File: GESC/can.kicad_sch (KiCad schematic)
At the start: 7 parts, among them J8 CAN, U5 SN65HVD230DR

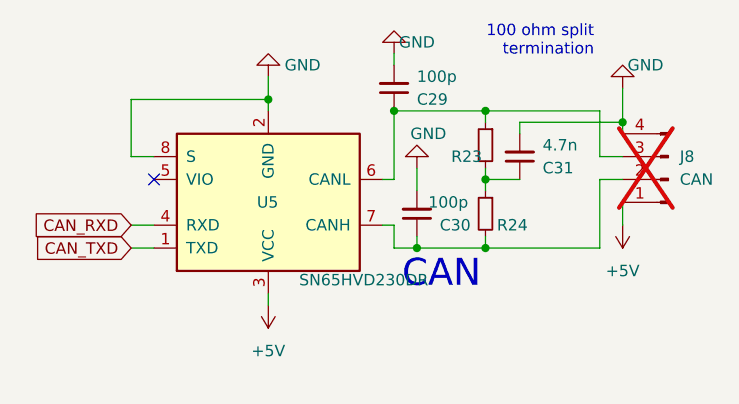
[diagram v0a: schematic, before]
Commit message: full to power board only
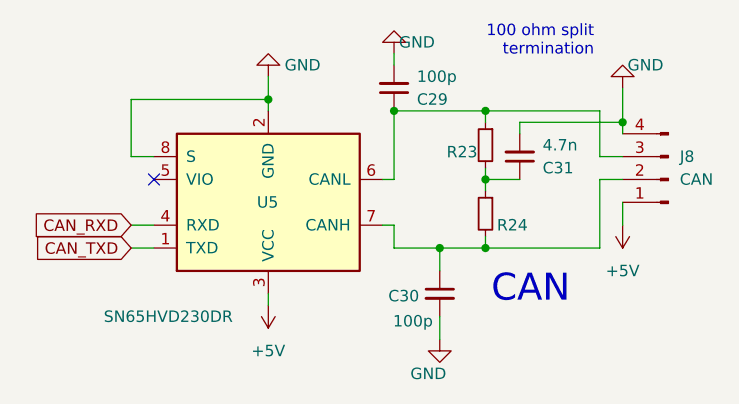
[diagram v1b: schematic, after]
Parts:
- J8: footprint Connector_JST:JST_PH_B4B-PH-K_1x04_P2.00mm_Vertical -> Connector_JST:JST_GH_BM04B-GHS-TBT_1x04-1MP_P1.25mm_Vertical; now fitted
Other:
- moved on the sheet: C30
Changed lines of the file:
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@@
+	)
+	(junction
+		(at 111.76 71.12)
+		(diameter 0)
+		(color 0 0 0 0)
 	)
 	(junction
@@
 		(color 0 0 0 0)
 	)
-	(junction
-		(at 109.22 71.12)
-		(diameter 0)
-		(color 0 0 0 0)
-	)
 	(no_connect
 		(at 80.01 63.5)
@@
 	(wire
 		(pts
-			(xy 109.22 71.12) (xy 106.68 71.12)
-		)
-		(stroke
-			(width 0)
-			(type default)
-		)
-	)
-	(wire
-		(pts
 			(xy 77.47 68.58) (xy 80.01 68.58)
 		)
@@
 	(wire
 		(pts
-			(xy 109.22 64.77) (xy 109.22 62.23)
-		)
-		(stroke
-			(width 0)
-			(type default)
-		)
-	)
-	(wire
-		(pts
 			(xy 116.84 71.12) (xy 116.84 69.85)
 		)
@@
 	(wire
 		(pts
-			(xy 109.22 71.12) (xy 109.22 69.85)
+			(xy 111.76 71.12) (xy 116.84 71.12)
 		)
 		(stroke
@@
 	(wire
 		(pts
+			(xy 111.76 71.12) (xy 111.76 73.66)
+		)
+		(stroke
+			(width 0)
+			(type default)
+		)
+	)
+	(wire
+		(pts
 			(xy 105.41 68.58) (xy 106.68 68.58)
 		)
@@
 	(wire
 		(pts
-			(xy 116.84 71.12) (xy 109.22 71.12)
+			(xy 106.68 71.12) (xy 111.76 71.12)
+		)
+		(stroke
+			(width 0)
+			(type default)
+		)
+	)
+	(wire
+		(pts
+			(xy 111.76 78.74) (xy 111.76 81.28)
 		)
 		(stroke
@@
 	(text "CAN"
 		(exclude_from_sim no)
-		(at 116.332 75.819 0)
+		(at 126.238 77.47 0)
 		(effects
 			(font
@@
 	(symbol
 		(lib_id "power:GND")
-		(at 109.22 62.23 180)
+		(at 111.76 81.28 0)
 		(unit 1)
 		(exclude_from_sim no)
@@
 		(dnp no)
 		(property "Reference" "#PWR027"
-			(at 109.22 55.88 0)
+			(at 111.76 87.63 0)
 			(effects
 				(font
@@
 		)
 		(property "Value" "GND"
-			(at 110.49 58.42 0)
+			(at 110.49 85.09 0)
 			(effects
 				(font
@@
 		)
 		(property "Footprint" ""
-			(at 109.22 62.23 0)
+			(at 111.76 81.28 0)
 			(effects
 				(font
@@
 		)
 		(property "Datasheet" ""
-			(at 109.22 62.23 0)
+			(at 111.76 81.28 0)
 			(effects
 				(font
@@
 		)
 		(property "Description" ""
-			(at 109.22 62.23 0)
+			(at 111.76 81.28 0)
 			(effects
 				(font
@@
 	(symbol
 		(lib_id "Device:C_Small")
-		(at 109.22 67.31 0)
-		(mirror x)
+		(at 111.76 76.2 0)
+		(mirror y)
 		(unit 1)
 		(exclude_from_sim no)
@@
 		(dnp no)
 		(property "Reference" "C30"
-			(at 111.76 68.58 0)
+			(at 109.474 76.454 0)
 			(effects
 				(font
@@
 		)
 		(property "Value" "100p"
-			(at 110.49 66.04 0)
+			(at 110.998 79.248 0)
 			(effects
 				(font
@@
 		)
 		(property "Footprint" "Capacitor_SMD:C_0402_1005Metric"
-			(at 109.22 67.31 0)
+			(at 111.76 76.2 0)
 			(effects
 				(font
@@
 		)
 		(property "Datasheet" ""
-			(at 109.22 67.31 0)
+			(at 111.76 76.2 0)
 			(effects
 				(font
@@
 		)
 		(property "Description" ""
-			(at 109.22 67.31 0)
+			(at 111.76 76.2 0)
 			(effects
 				(font
@@
 		)
 		(property "LCSC" "C1546"
-			(at 109.22 67.31 0)
+			(at 111.76 76.2 0)
 			(effects
 				(font
@@
 		(dnp no)
 		(property "Reference" "R23"
-			(at 113.03 60.96 0)
+			(at 112.522 60.452 0)
 			(effects
 				(font
@@
 		(in_bom yes)
 		(on_board yes)
-		(dnp yes)
+		(dnp no)
 		(fields_autoplaced yes)
 		(property "Reference" "J8"
@@
 			)
 		)
-		(property "Footprint" "Connector_JST:JST_PH_B4B-PH-K_1x04_P2.00mm_Vertical"
+		(property "Footprint" "Connector_JST:JST_GH_BM04B-GHS-TBT_1x04-1MP_P1.25mm_Vertical"
 			(at 137.16 63.5 0)
 			(effects
@@
 		)
 		(instances
-			(project "GESC"
+			(project ""
+				(path "/dc289c68-d15f-4833-9b73-29cf7cb2a289/52d04b8d-c40b-425a-8466-d9c480f0fea8"
+					(reference "J8")
+					(unit 1)
+				)
 				(path "/dc289c68-d15f-4833-9b73-29cf7cb2a289/82f3b7eb-8bd6-4bcb-bda1-a40c2d94d125"
 					(reference "J8")
@@
 		)
 		(property "Value" "SN65HVD230DR"
-			(at 96.139 74.676 0)
-			(effects
-				(font
+			(at 74.422 78.74 0)
+			(effects
+				(font
